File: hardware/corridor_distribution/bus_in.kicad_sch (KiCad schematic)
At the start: 20 parts, among them J10 Screw_Terminal_01x04, J12 Conn_02x03_Odd_Even, Q1 Q_Dual_NMOS_S1G1D2S2G2D1, U6 P82B96

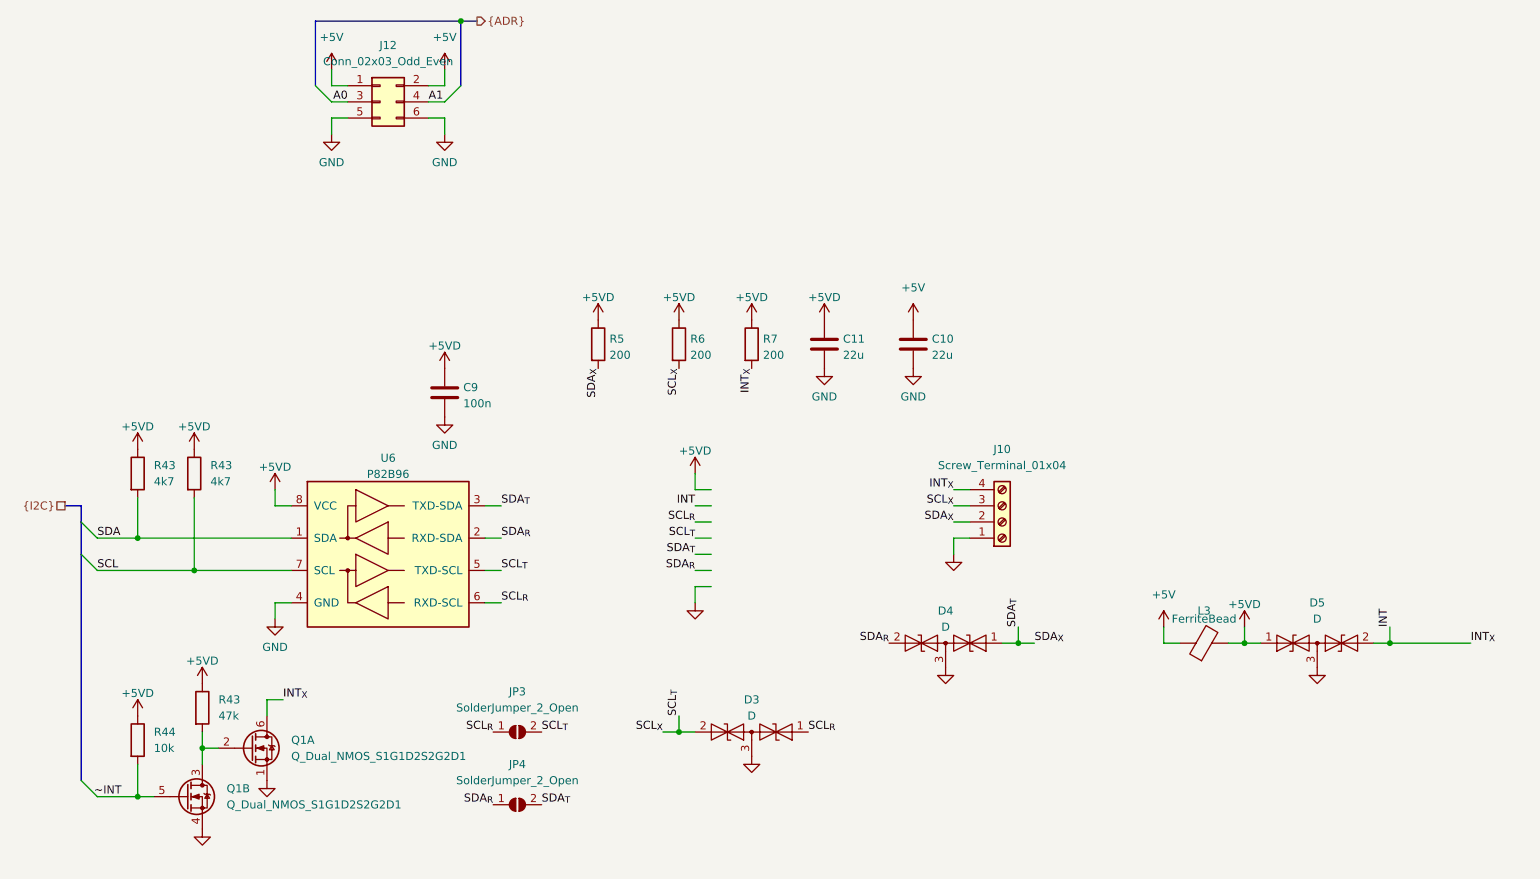
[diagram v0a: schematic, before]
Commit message: led balance and corridor ready
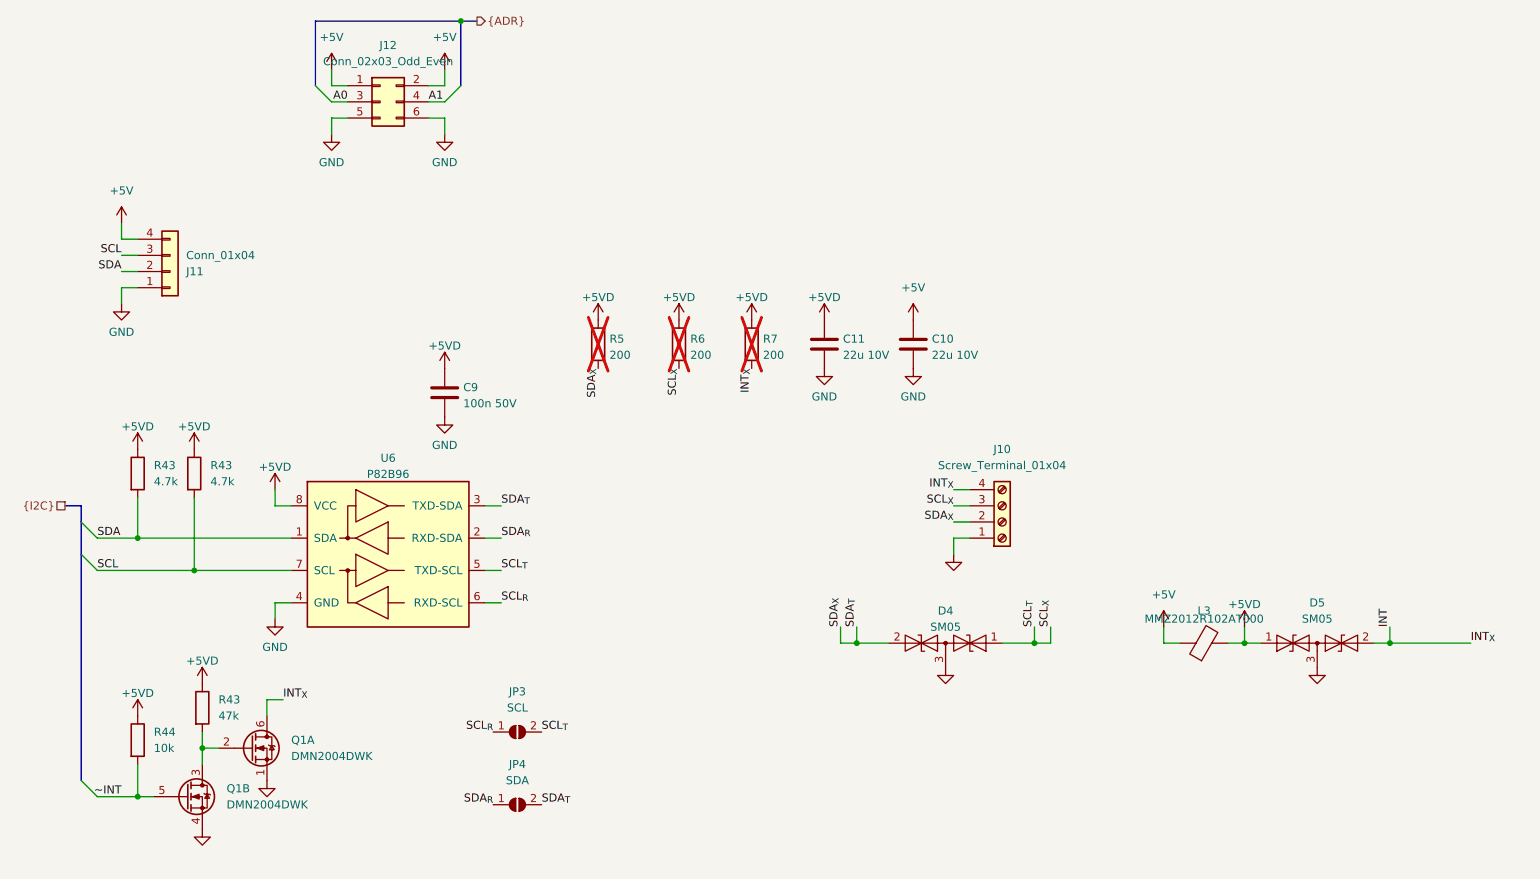
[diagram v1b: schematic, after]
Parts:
- removed D3: D, Package_TO_SOT_SMD:SOT-23_Handsoldering, symbol Diode:SM712_SOT23
- added J11: Conn_01x04, Connector_PinHeader_2.54mm:PinHeader_1x04_P2.54mm_Vertical, symbol Connector_Generic:Conn_01x04
- C10, C11: value 22u -> 22u 10V; LCSC Part # (none) -> C29277; Total quantity (none) -> 50
- C9: value 100n -> 100n 50V; LCSC Part # (none) -> C14663; Total quantity (none) -> 30
- D4, D5: value D -> SM05; LCSC Part # (none) -> C460613; Total quantity (none) -> 100
- J10, J12: now left out of the parts list
- JP3: value SolderJumper_2_Open -> SCL
- JP4: value SolderJumper_2_Open -> SDA
- L3: value FerriteBead -> MMZ2012R102AT000; LCSC Part # (none) -> C76810; Total quantity (none) -> 5
- Q1: value Q_Dual_NMOS_S1G1D2S2G2D1 -> DMN2004DWK; LCSC Part # (none) -> C156343; Total quantity (none) -> 5
- R43: value 4k7 -> 4.7k; LCSC Part # (none) -> C99782; Total quantity (none) -> 10
- R43: LCSC Part # (none) -> C105579; Total quantity (none) -> 5
- R44: LCSC Part # (none) -> C98220; Total quantity (none) -> 10
- R5, R6, R7: LCSC Part # (none) -> C114567; Total quantity (none) -> 15; now not fitted
- U6: LCSC Part # (none) -> C2687855; Total quantity (none) -> 5
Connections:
- net +5V: now also J11.4 (Pin_4)
- net GND: now also J11.1 (Pin_1)
- net SCL: now also J11.3 (Pin_3)
- net SCL_{T}: now also D4.1 (A1)
- net SDA: now also J11.2 (Pin_2)
- net SDA_{R}: no longer D4.2 (A2)
- net SDA_{T}: now also D4.2 (A2); no longer D4.1 (A1)

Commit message: Night Light firmware
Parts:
- added D22, D23, D3: D_Schottky, symbol Device:D_Schottky
- R5, R6, R7: value 200 -> 330
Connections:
- net +5VD: now also D22.1 (K), D23.1 (K), D3.1 (K)
- net INT: now also D23.2 (A)
- net SCL_{T}: now also D22.2 (A)
- net SDA_{T}: now also D3.2 (A)
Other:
- moved on the sheet: R5, R6, R7
